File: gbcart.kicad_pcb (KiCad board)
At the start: 2 copper layers, 51.4 x 61 mm, 34 parts, among them J1 Conn_01x32, J2 USB_B_Micro, J3 Micro_SD_Card, U1 ATmega32U4-A, U2 74HC138, U3 74HCT1G125, U4 74LS259, U5 29F040-TSOP-SP, U6 74lxc125, U7 74HCT1G125, U8 LD3985M33R_SOT23, U9 NC7SZ08, Y1 16MHz

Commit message: DEV revision
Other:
- board text added: "DEV"
- board text removed: "v1.0"
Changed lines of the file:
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@@
   (gr_line locked (start 149.525 62.595) (end 145.525 62.595) (layer "Edge.Cuts") (width 0.15))
   (gr_line locked (start 99.225 112.395) (end 98.125 112.395) (layer "Edge.Cuts") (width 0.15))
-  (gr_text "v1.0" (at 141.732 97.79) (layer "B.Cu")
+  (gr_text "DEV" (at 141.732 97.79) (layer "B.Cu")
     (effects (font (size 1.5 1.5) (thickness 0.3)) (justify mirror))
   )

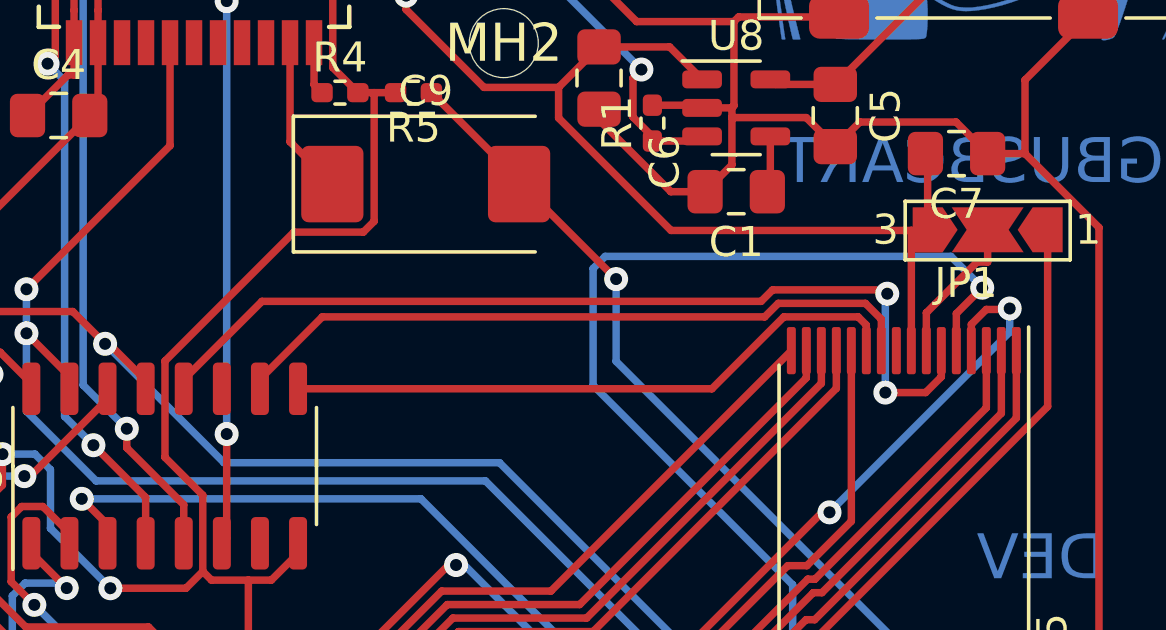
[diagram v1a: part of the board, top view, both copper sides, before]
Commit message: Add forgotten connection to A18
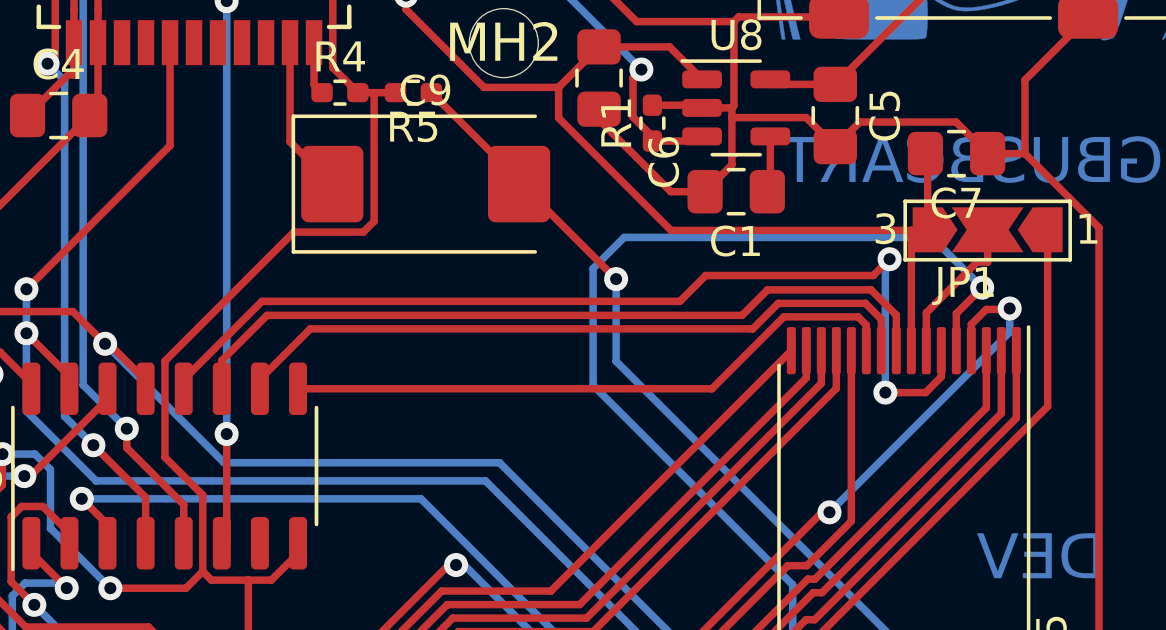
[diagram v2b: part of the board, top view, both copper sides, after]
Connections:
- U4 pad 11: unconnected-(U4-Pad11) -> Net-(U4-Pad11)
- U5 pad 9: unconnected-(U5-Pad9) -> Net-(U4-Pad11)
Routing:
- net Net-(U4-Pad11): track 0.00 -> 25.9 mm
- net Net-(U4-Pad12): track 31.3 -> 33.0 mm
- net /GB.A14: track 76.9 -> 77.4 mm

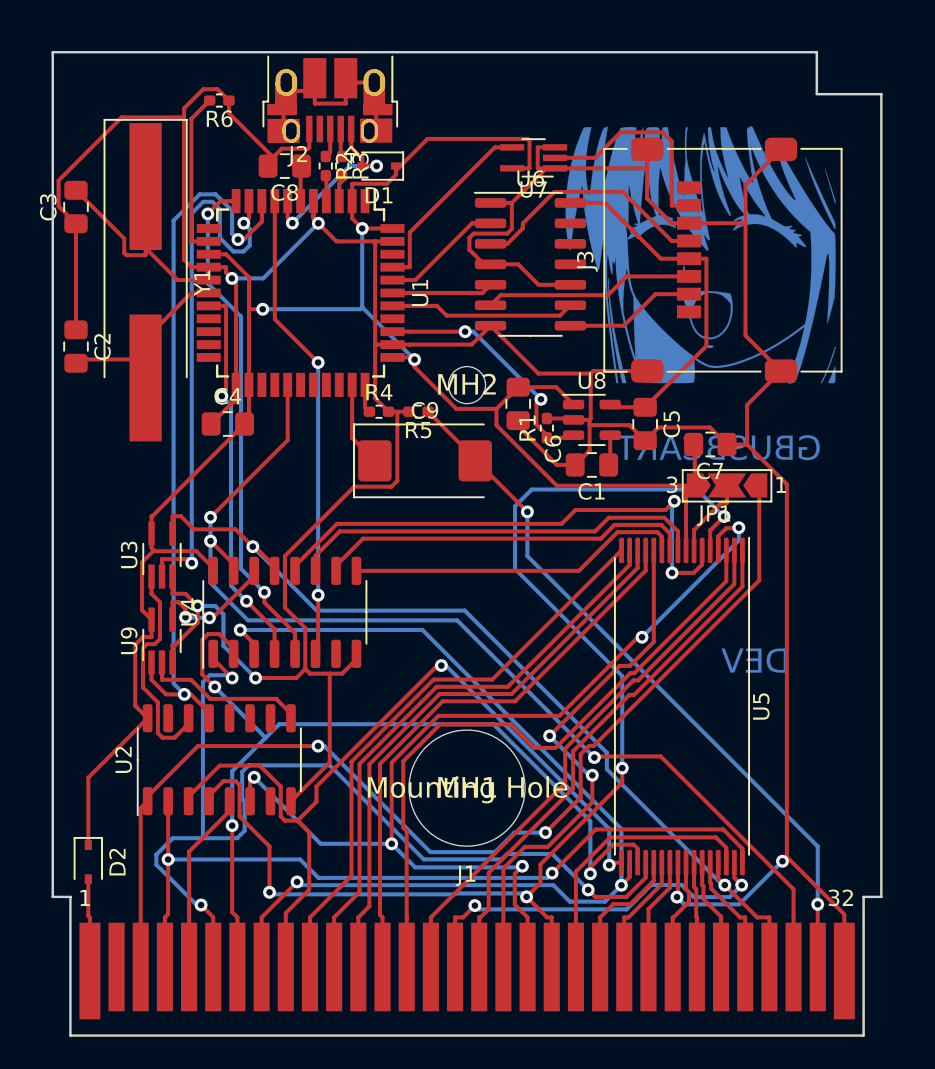
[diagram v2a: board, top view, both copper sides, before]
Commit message: Add LED and switch
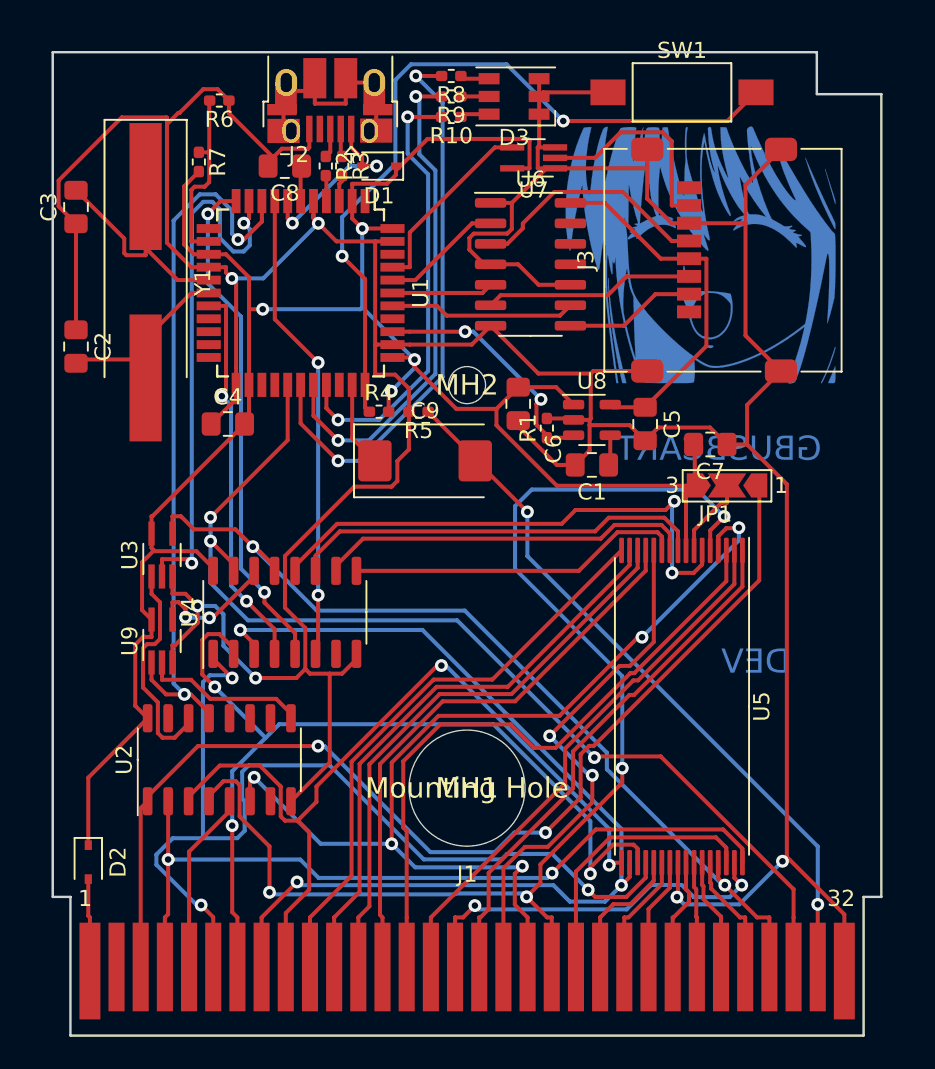
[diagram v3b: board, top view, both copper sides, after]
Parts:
- added D3: LED_RGB, LED_SMD:LED_RGB_PLCC-6, F.Cu at (126.7, 62.7)
- added R10: 330, Resistor_SMD:R_0402_1005Metric_Pad0.72x0.64mm_HandSolder, F.Cu at (122.8, 64.0)
- added R7: 10k, Resistor_SMD:R_0402_1005Metric_Pad0.72x0.64mm_HandSolder, F.Cu at (107.2, 66.8)
- added R8: 330, Resistor_SMD:R_0402_1005Metric_Pad0.72x0.64mm_HandSolder, F.Cu at (122.8, 61.5)
- added R9: 330, Resistor_SMD:R_0402_1005Metric_Pad0.72x0.64mm_HandSolder, F.Cu at (122.8, 62.7)
- added SW1: SW_Push, Button_Switch_SMD:SW_SPST_FSMSM, F.Cu at (137.2, 62.5)
- R4: value 0 -> 10k
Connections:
- R4 pad 2: GND -> +5V
- U1 pad 28: unconnected-(U1-Pad28) -> Net-(U1-Pad28)
- U1 pad 29: unconnected-(U1-Pad29) -> Net-(U1-Pad29)
- U1 pad 30: unconnected-(U1-Pad30) -> Net-(U1-Pad30)
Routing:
- net Net-(R4-Pad1): track 1.78 -> 47.6 mm, vias 0 -> 2
- net Net-(U1-Pad28): track 0.00 -> 35.3 mm, vias 0 -> 2
- net Net-(U1-Pad29): track 0.00 -> 31.1 mm, vias 0 -> 2
- net Net-(U1-Pad30): track 0.00 -> 27.7 mm, vias 0 -> 2
- net +5V: track 120.5 -> 131.1 mm, vias 3 -> 4
- net GND: track 276.3 -> 285.5 mm
- net Net-(D3-Pad6): track 0.00 -> 1.82 mm
- net Net-(D3-Pad4): track 0.00 -> 1.82 mm
- net Net-(D3-Pad5): track 0.00 -> 1.75 mm
- net Net-(R6-Pad2): track 10.3 -> 11.3 mm

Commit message: Mark proper 74 family
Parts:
- U4: value 74LS259 -> 74HC259
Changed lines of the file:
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@@
       (effects (font (size 1 1) (thickness 0.15)))
     )
-    (fp_text value "74LS259" (at 0 5.9 90) (layer "F.Fab")
+    (fp_text value "74HC259" (at 0 5.9 90) (layer "F.Fab")
       (effects (font (size 1 1) (thickness 0.15)))
     )

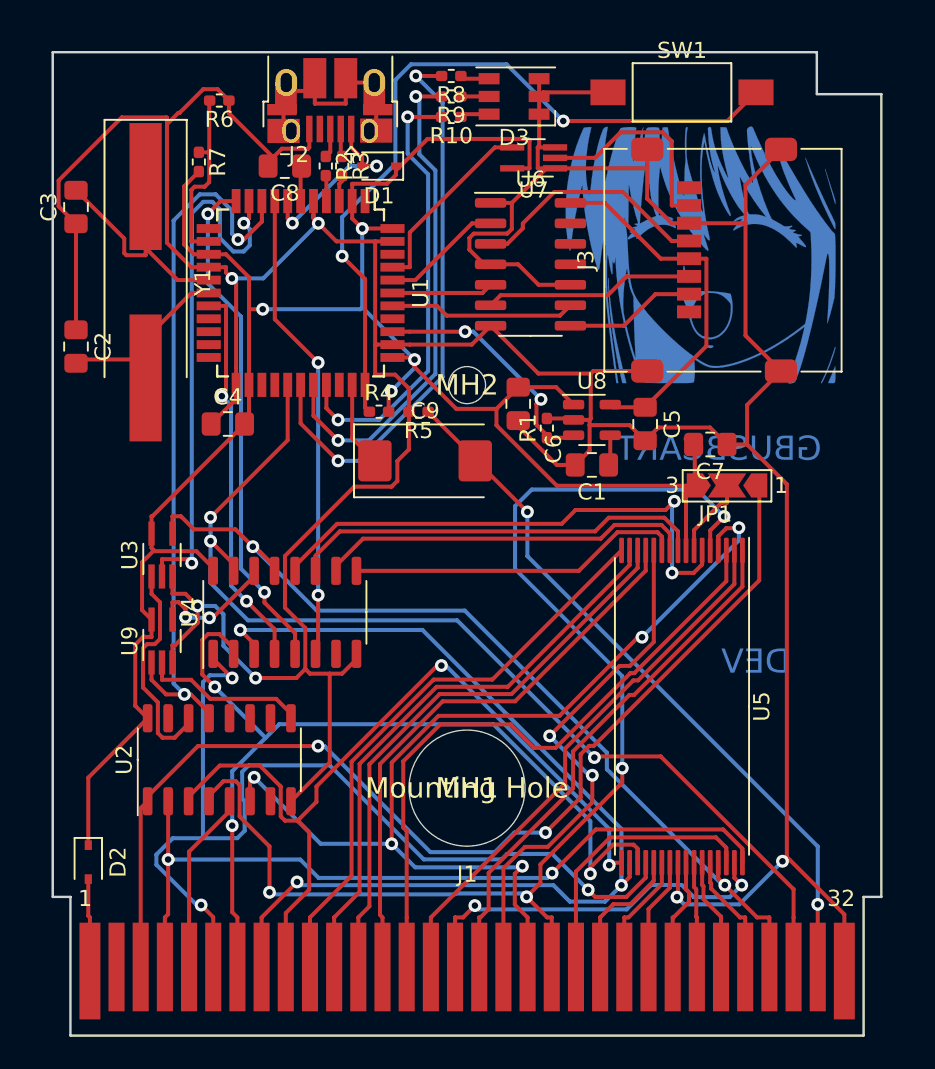
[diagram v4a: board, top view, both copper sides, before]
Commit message: choose diferent mcu
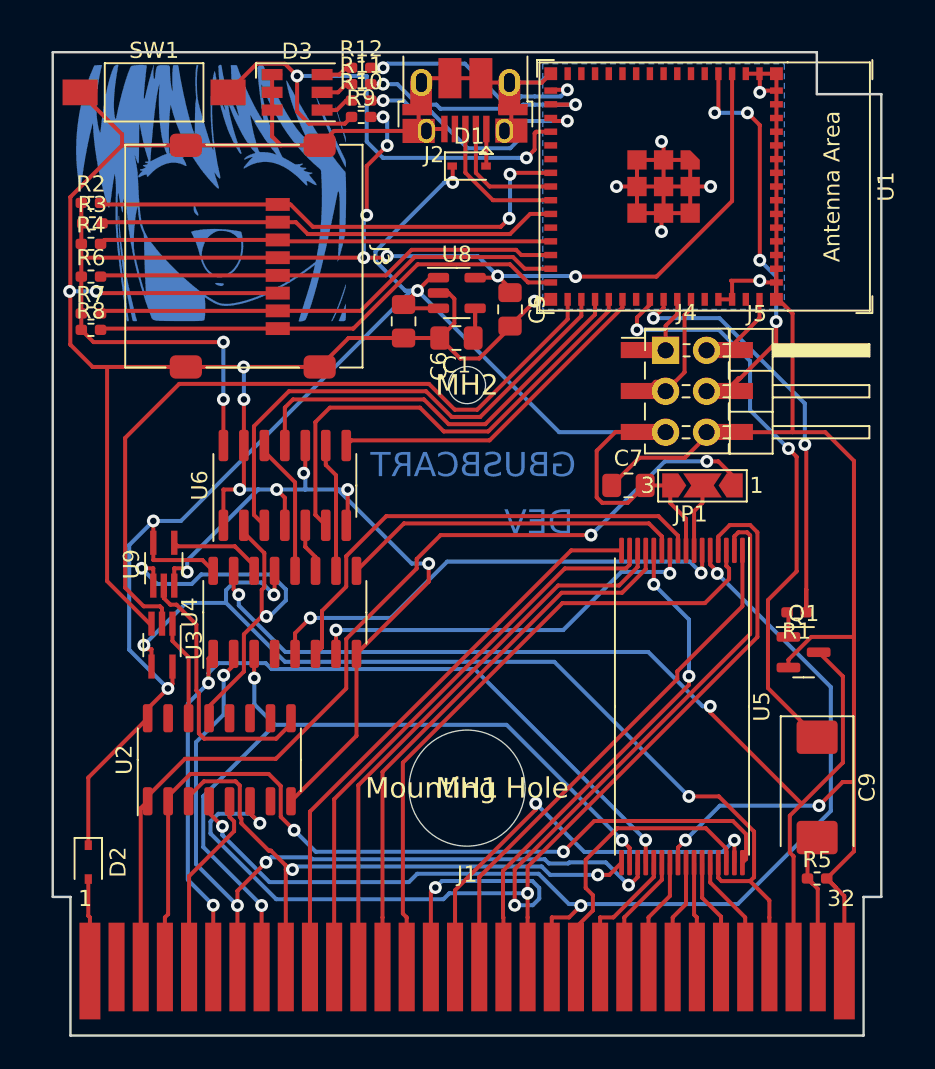
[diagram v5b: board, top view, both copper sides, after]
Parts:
- removed C2, C3: 22pF, Capacitor_SMD:C_0805_2012Metric_Pad1.18x1.45mm_HandSolder
- removed C4: 100nF, Capacitor_SMD:C_0805_2012Metric_Pad1.18x1.45mm_HandSolder
- removed C8: 1µF, Capacitor_SMD:C_0805_2012Metric_Pad1.18x1.45mm_HandSolder
- removed U7: 74HCT1G125, Package_TO_SOT_SMD:SOT-353_SC-70-5_Handsoldering
- removed Y1: 16MHz, Crystal:Crystal_SMD_HC49-SD_HandSoldering
- added J4: Conn_01x06_Male, Connector_PinHeader_2.54mm:PinHeader_2x03_P2.54mm_Vertical_SMD, F.Cu at (137.5, 81.0)
- added J5: Conn_01x06_Male, Connector_PinHeader_2.54mm:PinHeader_2x03_P2.54mm_Horizontal, F.Cu at (136.1, 78.5)
- added Q1: BC847, Package_TO_SOT_SMD:SOT-23, F.Cu at (144.7, 97.2)
- added R11: 330, Resistor_SMD:R_0402_1005Metric_Pad0.72x0.64mm_HandSolder, F.Cu at (117.3, 62.0)
- added R12: 330, Resistor_SMD:R_0402_1005Metric_Pad0.72x0.64mm_HandSolder, F.Cu at (117.3, 61.0)
- R1: value 1k -> 10k
- R2, R3: value 22 -> 10k
- R6: value DNP -> 10k
- R8, R9: value 330 -> 10k
- U1: value ATmega32U4-A -> ESP32-S3-MINI-1; footprint Package_QFP:TQFP-44_10x10mm_P0.8mm -> Espressif:ESP32-S3-MINI-1
- moved R5 38.1 mm to (145.5, 111.3), turned to 0 degrees
- moved SW1 32.7 mm to (104.4, 62.5)
- moved C9 31.7 mm to (145.5, 105.6), turned to -90 degrees
- moved REF** 30.6 mm to (108.1, 79.2)
- moved J3 29.7 mm to (110.0, 72.6), turned to -90 degrees
- moved R8 27.3 mm to (100.5, 77.2), turned to 0 degrees
- moved U1 23.5 mm to (136.0, 68.3)
- moved R4 20.7 mm to (100.5, 71.9)
- moved U6 20.5 mm to (112.5, 86.9), turned to 90 degrees
- moved R1 19.3 mm to (144.3, 94.7), turned to 180 degrees
- moved R3 15.9 mm to (100.6, 70.6), turned to 0 degrees
- moved R2 14.7 mm to (100.5, 69.3), turned to 0 degrees
- moved R6 13.5 mm to (100.5, 73.9), turned to 0 degrees
- moved D3 13.5 mm to (113.3, 62.5), turned to 0 degrees
- moved R7 11.5 mm to (100.5, 76.2), turned to 0 degrees
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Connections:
- J2 pad 6: unconnected-(J2-Pad6) -> GND
- J3 pad 1: unconnected-(J3-Pad1) -> /SD_DATA2
- J3 pad 2: Net-(J3-Pad2) -> /SD_DATA3
- J3 pad 3: Net-(J3-Pad3) -> /SD_CMD
- J3 pad 5: Net-(J3-Pad5) -> /SD_CLOCK
- J3 pad 7: Net-(J3-Pad7) -> /SD_DATA0
- J3 pad 8: unconnected-(J3-Pad8) -> /SD_DATA1
- R1 pad 2: GND -> Net-(Q1-Pad1)
- R10 pad 1: Net-(D3-Pad6) -> Net-(D3-Pad4)
- R10 pad 2: Net-(U1-Pad30) -> /L_B
- R2 pad 1: Net-(J2-Pad3) -> +3.3V
- R2 pad 2: Net-(R2-Pad2) -> /SD_DATA2
- R3 pad 1: Net-(J2-Pad2) -> +3.3V
- R3 pad 2: Net-(R3-Pad2) -> /SD_DATA3
- R4 pad 1: Net-(R4-Pad1) -> +3.3V
- R4 pad 2: +5V -> /SD_CMD
- R6 pad 1: GND -> +3.3V
- R6 pad 2: Net-(R6-Pad2) -> /SD_CLOCK
- R7 pad 1: Net-(R6-Pad2) -> +3.3V
- R7 pad 2: +5V -> /SD_DATA0
- R8 pad 1: Net-(D3-Pad4) -> +3.3V
- R8 pad 2: Net-(U1-Pad28) -> /SD_DATA1
- R9 pad 1: Net-(D3-Pad5) -> /BTN
- R9 pad 2: Net-(U1-Pad29) -> +3.3V
- SW1 pad 2: Net-(R4-Pad1) -> /BTN
- U1 pad 1: unconnected-(U1-Pad1) -> GND
- U1 pad 10: /MOSI -> unconnected-(U1-Pad10)
- U1 pad 11: /MISO -> unconnected-(U1-Pad11)
- U1 pad 13: Net-(R6-Pad2) -> unconnected-(U1-Pad13)
- U1 pad 14: +5V -> unconnected-(U1-Pad14)
- U1 pad 15: GND -> unconnected-(U1-Pad15)
- U1 pad 16: Net-(C3-Pad2) -> /L_R
- U1 pad 17: Net-(C2-Pad2) -> /L_G
- U1 pad 18: /IRQ -> /L_B
- U1 pad 19: unconnected-(U1-Pad19) -> /BTN
- U1 pad 2: +5V -> GND
- U1 pad 22: unconnected-(U1-Pad22) -> /SD_DATA2
- U1 pad 23: GND -> Net-(J2-Pad2)
- U1 pad 24: +5V -> Net-(J2-Pad3)
- U1 pad 25: unconnected-(U1-Pad25) -> /SD_DATA3
- U1 pad 27: /GB.~{RST} -> /SD_CMD
- U1 pad 28: Net-(U1-Pad28) -> /SD_CLOCK
- U1 pad 29: Net-(U1-Pad29) -> /SD_DATA0
- U1 pad 3: Net-(R3-Pad2) -> +3.3V
- U1 pad 30: Net-(U1-Pad30) -> /SD_DATA1
- U1 pad 31: unconnected-(U1-Pad31) -> /MOSI
- U1 pad 32: Net-(C9-Pad1) -> Net-(U6-Pad3)
- U1 pad 33: Net-(R4-Pad1) -> Net-(U6-Pad11)
- U1 pad 34: +5V -> Net-(U1-Pad34)
- U1 pad 35: GND -> Net-(U1-Pad35)
- U1 pad 36: Net-(R1-Pad1) -> unconnected-(U1-Pad36)
- U1 pad 37: unconnected-(U1-Pad37) -> Net-(C9-Pad1)
- U1 pad 38: Net-(U1-Pad38) -> Net-(R1-Pad1)
- U1 pad 39: Net-(U1-Pad39) -> /DTX_E
- U1 pad 4: Net-(R2-Pad2) -> /DDTR
- U1 pad 40: Net-(U1-Pad40) -> /DRX_E
- U1 pad 41: Net-(U1-Pad41) -> unconnected-(U1-Pad41)
- U1 pad 42: unconnected-(U1-Pad42) -> GND
- U1 pad 44: +5V -> unconnected-(U1-Pad44)
- U1 pad 5: GND -> unconnected-(U1-Pad5)
- U1 pad 6: Net-(C8-Pad1) -> unconnected-(U1-Pad6)
- U1 pad 7: Net-(D1-Pad2) -> unconnected-(U1-Pad7)
- U1 pad 8: /SS -> unconnected-(U1-Pad8)
- U1 pad 9: /SCL -> unconnected-(U1-Pad9)
- U4 pad 10: Net-(U4-Pad10) -> /IRQ
- U4 pad 11: Net-(U4-Pad11) -> /SS
- U4 pad 12: Net-(U4-Pad12) -> /MISO
- U4 pad 4: /IRQ -> unconnected-(U4-Pad4)
- U4 pad 5: /MISO -> Net-(U4-Pad5)
- U4 pad 6: /SS -> Net-(U4-Pad6)
- U4 pad 7: unconnected-(U4-Pad7) -> Net-(U4-Pad7)
- U5 pad 10: Net-(U4-Pad10) -> Net-(U4-Pad7)
- U5 pad 6: Net-(U4-Pad12) -> Net-(U4-Pad5)
- U5 pad 9: Net-(U4-Pad11) -> Net-(U4-Pad6)
- U6 pad 11: (no net) -> Net-(U6-Pad11)
- U6 pad 12: (no net) -> /MISO
- U6 pad 13: (no net) -> GND
- U6 pad 2: Net-(U1-Pad40) -> /SCL
- U6 pad 3: Net-(J3-Pad5) -> Net-(U6-Pad3)
- U6 pad 5: Net-(U1-Pad39) -> /SS
- U6 pad 6: Net-(J3-Pad3) -> Net-(U1-Pad34)
- U6 pad 8: Net-(J3-Pad2) -> Net-(U1-Pad35)
- U6 pad 9: Net-(U1-Pad38) -> /IRQ
- U8 pad 3: Net-(R1-Pad1) -> +5V
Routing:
- net +3.3V: track 22.9 -> 87.3 mm, vias 0 -> 9
- net Net-(R4-Pad1): track 47.6 -> 0.00 mm, vias 2 -> 0
- net Net-(U1-Pad28): track 35.3 -> 0.00 mm, vias 2 -> 0
- net /GB.AUDIO: track 44.5 -> 11.4 mm, vias 2 -> 0
- net Net-(U4-Pad12): track 33.0 -> 0.00 mm, vias 2 -> 0
- net /BTN: track 0.00 -> 32.9 mm, vias 0 -> 2
- net GND: track 285.5 -> 318.2 mm, vias 6 -> 19
- net Net-(U6-Pad3): track 0.00 -> 31.9 mm
- net /SD_DATA2: track 0.00 -> 31.6 mm, vias 0 -> 2
- net Net-(C9-Pad1): track 5.30 -> 36.6 mm, vias 0 -> 2
- net Net-(U1-Pad29): track 31.1 -> 0.00 mm, vias 2 -> 0
- net /SD_DATA1: track 0.00 -> 30.1 mm
- net Net-(U4-Pad5): track 0.00 -> 30.0 mm, vias 0 -> 2
- net Net-(U4-Pad6): track 0.00 -> 29.9 mm
- net /SD_DATA0: track 0.00 -> 29.7 mm
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- added copper zone on B.Cu, net GND
